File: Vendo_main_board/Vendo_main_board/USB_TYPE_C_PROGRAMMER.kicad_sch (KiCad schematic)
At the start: 11 parts, among them Q10 BSS138, Q9 BSS138, U17 CH340C

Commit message: -update schematic
-recheck lcsc part number ,value
-check and update footprint assignment
-add load switch for the wdt and ldo combination

-add link for quick connect footprint must be discuss for clarification
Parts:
- USB1: footprint SolX:USB-C-SMD_TYPE-C16PIN -> InnovKits:USB-C-SMD_TYPE-C16PIN

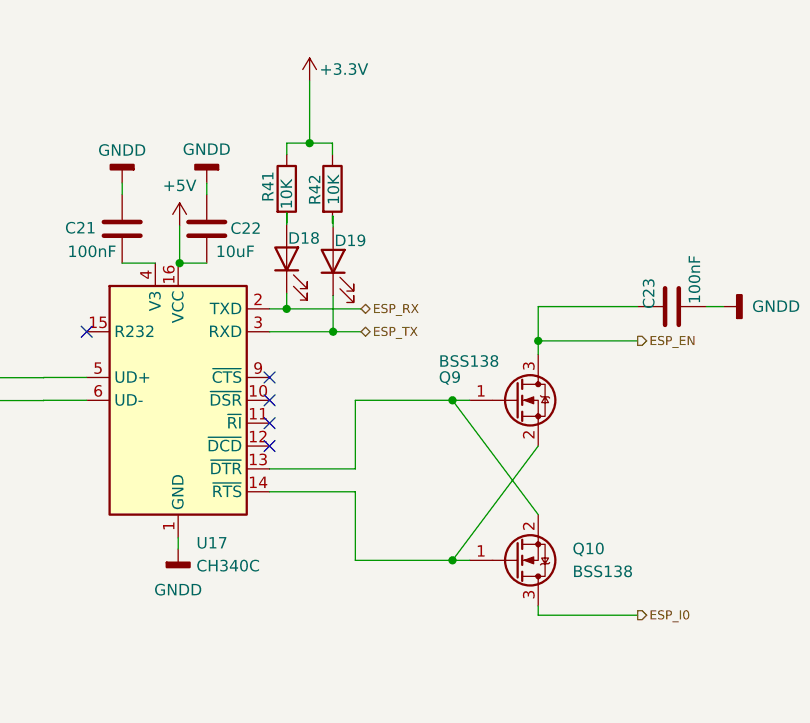
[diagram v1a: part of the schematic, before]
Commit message: -update scheme and pcb placement
update scheme and footprint
added spade connectors
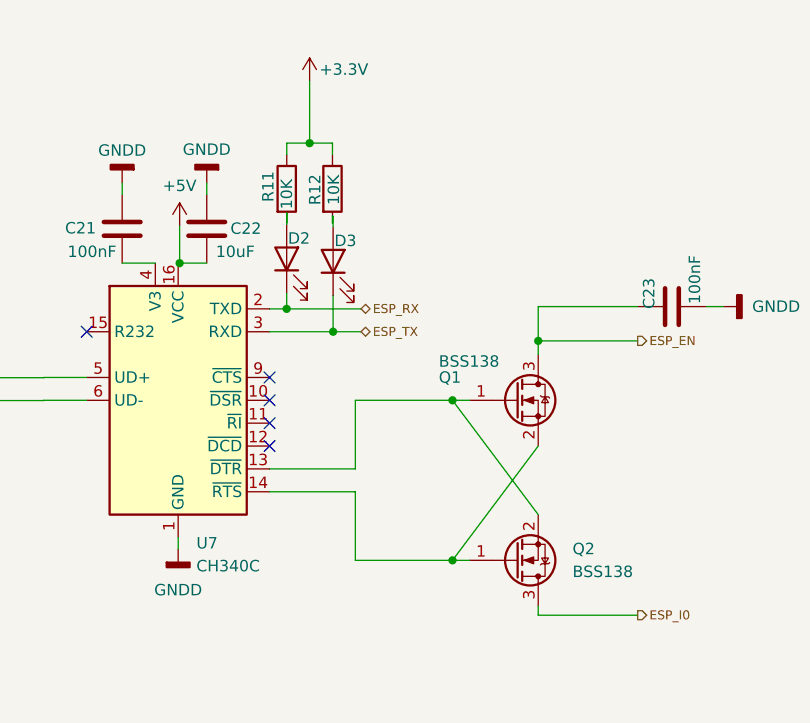
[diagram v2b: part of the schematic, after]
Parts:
- renumbered D18 to D2, D19 to D3, Q9 to Q1, Q10 to Q2, R41 to R11, R42 to R12, U17 to U7
